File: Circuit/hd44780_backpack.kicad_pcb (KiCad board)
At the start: 2 copper layers, 98.4 x 60.3 mm, 32 parts, among them IC1 ATTINY84A-SS, K1 PWR_SHIFT, M1 MESHTHING, P1 I2C, P2 ISCP, P3 ATTINY_BREAKOUT, P4 USB_5PIN_SHELL, P5 MESH_BKOUT_1-10, P6 MESH_BKOUT_11-20, P7 MESH_ENABLE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

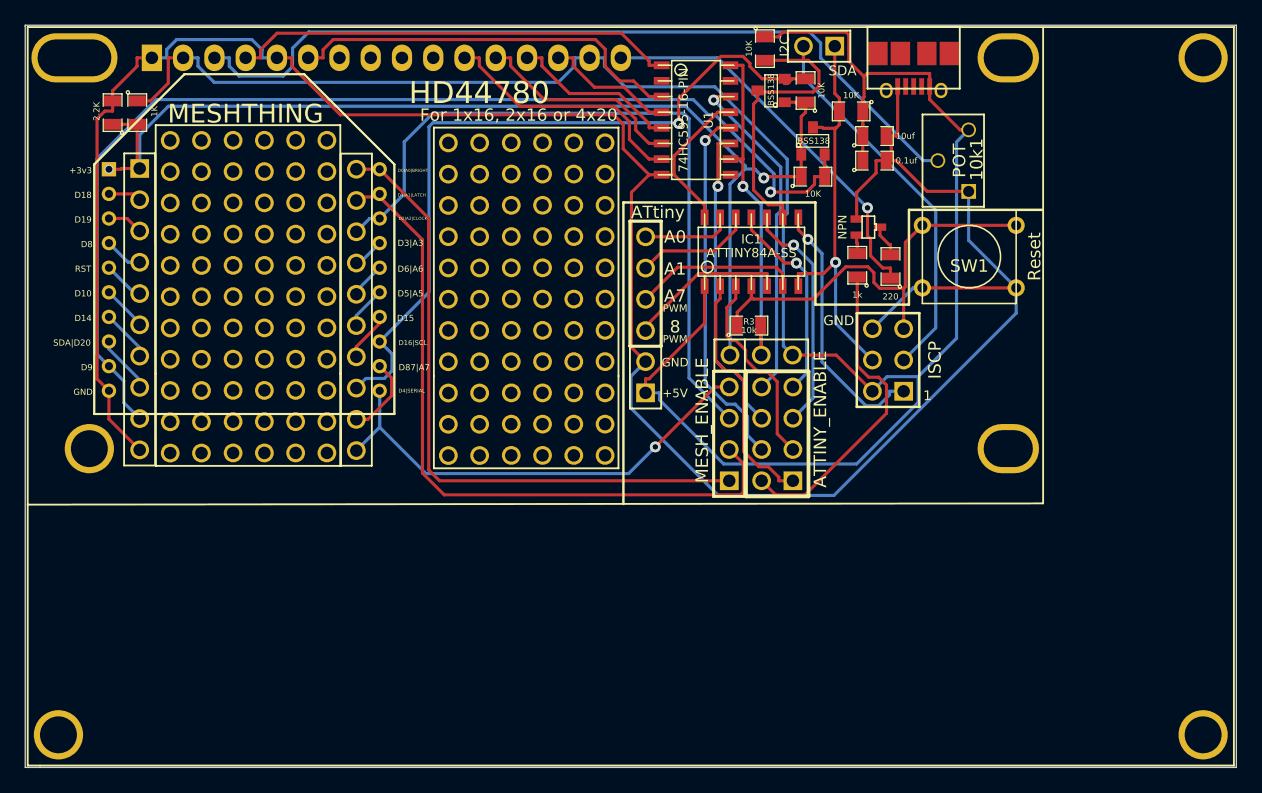
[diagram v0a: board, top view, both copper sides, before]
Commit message: Changed to using a BSS138DW
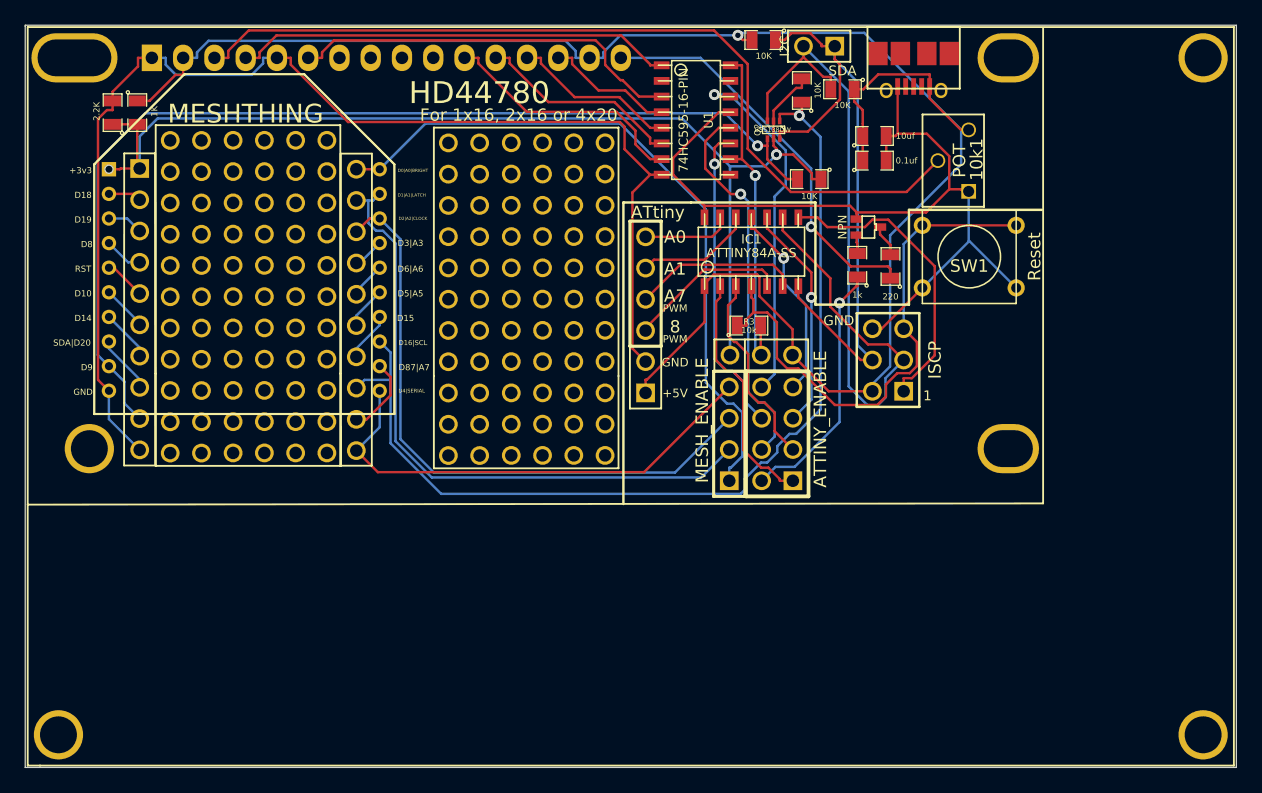
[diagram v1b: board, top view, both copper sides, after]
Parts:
- removed Q3: BSS138, SOT23
- Q2: value BSS138 -> BSS138DW; footprint SOT23 -> SOT363
- moved Q2 3.32 mm to (73.1, 20.8), turned to 180 degrees
- moved R4 1.93 mm to (78.7, 17.5)
- moved R6 0.71 mm to (72.3, 13.5), turned to 180 degrees
- moved R5 0.36 mm to (76.0, 24.8), turned to 180 degrees
- moved R7 0.30 mm to (75.4, 17.6)
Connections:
- IC1 pad 7: N-0000032 (its old number) -> N-0000055
- IC1 pad 9: N-0000019 (its old number) -> N-0000057
- M1 pad 13: N-0000022 (its old number) -> N-0000056
- M1 pad 9: N-0000033 (its old number) -> N-0000058
- P1 pad 1: N-0000032 (its old number) -> N-0000055
- P1 pad 2: N-0000019 (its old number) -> N-0000057
- P2 pad 3: N-0000019 (its old number) -> N-0000057
- P2 pad 4: N-0000032 (its old number) -> N-0000055
- P5 pad 2: N-0000033 (its old number) -> N-0000058
- P6 pad 8: N-0000022 (its old number) -> N-0000056
- Q2 pad 1: +3.3V -> N-0000056
- Q2 pad 2: N-0000033 (its old number) -> +3.3V
- Q2 pad 3: N-0000032 (its old number) -> N-0000057
- R4 pad 2: N-0000032 (its old number) -> N-0000057
- R5 pad 2: N-0000033 (its old number) -> N-0000058
- R6 pad 1: +5V -> N-0000055
- R6 pad 2: N-0000019 (its old number) -> +5V
- R7 pad 1: +3.3V -> N-0000056
- R7 pad 2: N-0000022 (its old number) -> +3.3V
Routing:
- net N-0000033 (its old number): track 90.7 -> 0.00 mm, vias 1 -> 0
- net N-0000058: track 0.00 -> 84.3 mm, vias 0 -> 1
- net N-0000056: track 0.00 -> 79.9 mm, vias 0 -> 1
- net N-0000057: track 0.00 -> 64.5 mm
- net N-0000022 (its old number): track 61.0 -> 0.00 mm, vias 1 -> 0
- net N-0000019 (its old number): track 55.6 -> 0.00 mm
- net N-0000055: track 0.00 -> 52.5 mm
- net N-0000032 (its old number): track 33.3 -> 0.00 mm, vias 1 -> 0
- net GND: track 204.5 -> 171.5 mm
- net +5V: track 181.2 -> 151.3 mm, vias 0 -> 1
- net N-0000023: track 35.1 -> 44.4 mm
- net N-0000033: track 59.4 -> 50.6 mm
- net N-000004: track 25.9 -> 20.7 mm, vias 0 -> 1
- net N-0000030: track 57.0 -> 52.2 mm
- net N-0000032: track 52.8 -> 56.9 mm
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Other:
- net class Default: clearance 0.254 -> 0.2; trace_width 0.254 -> 0.2
- rule trace_clearance: 0.254 -> 0.2
- rule trace_min: 0.254 -> 0.2

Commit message: problem with back masks
the meshthingy had no back mask area.  made it very difficult to solder.
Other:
- board text added: "Controller for HD4470 Screen Designed by John Spencer, 2014 https://github.com/mage0r/HD44780_Backpack Version 1.5 - Meshthingy Version"
- board text removed: "Controller for HD4470 Screen Designed by John Spencer, 2014 https://github.com/mage0r/HD44780_Backpack Version 1.4 - Meshthingy Version"
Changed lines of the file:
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@@
 (kicad_pcb (version 3) (host pcbnew "(2013-07-07 BZR 4022)-stable")
   (general
-    (links 101)
+    (links 0)
     (no_connects 0)
-    (area 12.249999 12.249999 110.750001 72.650001)
+    (area 12.05 10.575 110.775001 72.725001)
     (thickness 1.6)
     (drawings 18)
@@
     (15 F.Cu signal)
     (0 B.Cu signal)
-    (16 B.Adhes user)
-    (17 F.Adhes user)
+    (16 B.Adhes user hide)
+    (17 F.Adhes user hide)
     (18 B.Paste user)
     (19 F.Paste user)
@@
     (22 B.Mask user)
     (23 F.Mask user)
-    (24 Dwgs.User user)
-    (25 Cmts.User user)
-    (26 Eco1.User user)
-    (27 Eco2.User user)
-    (28 Edge.Cuts user)
+    (24 Dwgs.User user hide)
+    (25 Cmts.User user hide)
+    (26 Eco1.User user hide)
+    (27 Eco2.User user hide)
+    (28 Edge.Cuts user hide)
   )
   (setup
@@
     (mod_text_size 1 1)
     (mod_text_width 0.15)
-    (pad_size 1.524 1.524)
-    (pad_drill 1.016)
+    (pad_size 1.1684 1.1684)
+    (pad_drill 0.6604)
     (pad_to_mask_clearance 0)
     (aux_axis_origin 0 0)
@@
       (effects (font (size 1.778 1.778) (thickness 0.0889)))
     )
-    (fp_text value MESHTHING (at 0.1 -13.5) (layer F.SilkS)
+    (fp_text value MESHTHING (at 0 -14.4) (layer F.SilkS)
       (effects (font (size 1.524 1.524) (thickness 0.15)))
     )
@@
     )
     (pad 2 thru_hole circle (at -10.9982 -6.9977) (size 1.1684 1.1684) (drill 0.6604)
-      (layers *.Cu F.Paste F.SilkS F.Mask)
+      (layers *.Cu *.Mask F.Paste F.SilkS)
       (net 33 N-0000037)
     )
     (pad 3 thru_hole circle (at -10.9982 -4.99872) (size 1.1684 1.1684) (drill 0.6604)
-      (layers *.Cu F.Paste F.SilkS F.Mask)
+      (layers *.Cu *.Mask F.Paste F.SilkS)
       (net 34 N-0000038)
     )
     (pad 4 thru_hole circle (at -10.9982 -2.99974) (size 1.1684 1.1684) (drill 0.6604)
-      (layers *.Cu F.Paste F.SilkS F.Mask)
+      (layers *.Cu *.Mask F.Paste F.SilkS)
       (net 35 N-0000039)
     )
     (pad 5 thru_hole circle (at -10.9982 -0.99822) (size 1.1684 1.1684) (drill 0.6604)
-      (layers *.Cu F.Paste F.SilkS F.Mask)
+      (layers *.Cu *.Mask F.Paste F.SilkS)
       (net 31 N-0000035)
     )
     (pad 6 thru_hole circle (at -10.9982 0.99822) (size 1.1684 1.1684) (drill 0.6604)
-      (layers *.Cu F.Paste F.SilkS F.Mask)
+      (layers *.Cu *.Mask F.Paste F.SilkS)
       (net 37 N-0000040)
     )
     (pad 7 thru_hole circle (at -10.9982 2.99974) (size 1.1684 1.1684) (drill 0.6604)
-      (layers *.Cu F.Paste F.SilkS F.Mask)
+      (layers *.Cu *.Mask F.Paste F.SilkS)
       (net 38 N-0000041)
     )
     (pad 8 thru_hole circle (at -10.9982 4.99872) (size 1.1684 1.1684) (drill 0.6604)
-      (layers *.Cu F.Paste F.SilkS F.Mask)
+      (layers *.Cu *.Mask F.Paste F.SilkS)
       (net 39 N-0000042)
     )
     (pad 9 thru_hole circle (at -10.9982 6.9977) (size 1.1684 1.1684) (drill 0.6604)
-      (layers *.Cu F.Paste F.SilkS F.Mask)
+      (layers *.Cu *.Mask F.Paste F.SilkS)
       (net 44 N-0000058)
     )
     (pad 10 thru_hole circle (at -10.9982 8.99922) (size 1.1684 1.1684) (drill 0.6604)
-      (layers *.Cu F.Paste F.SilkS F.Mask)
+      (layers *.Cu *.Mask F.Paste F.SilkS)
       (net 3 GND)
     )
     (pad 11 thru_hole circle (at 10.9982 8.99922) (size 1.1684 1.1684) (drill 0.6604)
-      (layers *.Cu F.Paste F.SilkS F.Mask)
+      (layers *.Cu *.Mask F.Paste F.SilkS)
       (net 9 N-0000014)
     )
     (pad 12 thru_hole circle (at 10.9982 6.9977) (size 1.1684 1.1684) (drill 0.6604)
-      (layers *.Cu F.Paste F.SilkS F.Mask)
+      (layers *.Cu *.Mask F.Paste F.SilkS)
       (net 10 N-0000015)
     )
     (pad 13 thru_hole circle (at 10.9982 4.99872) (size 1.1684 1.1684) (drill 0.6604)
-      (layers *.Cu F.Paste F.SilkS F.Mask)
+      (layers *.Cu *.Mask F.Paste F.SilkS)
       (net 42 N-0000056)
     )
     (pad 14 thru_hole circle (at 10.9982 2.99974) (size 1.1684 1.1684) (drill 0.6604)
-      (layers *.Cu F.Paste F.SilkS F.Mask)
+      (layers *.Cu *.Mask F.Paste F.SilkS)
       (net 8 N-0000013)
     )
     (pad 15 thru_hole circle (at 10.9982 0.99822) (size 1.1684 1.1684) (drill 0.6604)
-      (layers *.Cu F.Paste F.SilkS F.Mask)
+      (layers *.Cu *.Mask F.Paste F.SilkS)
       (net 7 N-0000012)
     )
     (pad 16 thru_hole circle (at 10.9982 -0.99822) (size 1.1684 1.1684) (drill 0.6604)
-      (layers *.Cu F.Paste F.SilkS F.Mask)
+      (layers *.Cu *.Mask F.Paste F.SilkS)
       (net 30 N-0000034)
     )
     (pad 17 thru_hole circle (at 10.9982 -2.99974) (size 1.1684 1.1684) (drill 0.6604)
-      (layers *.Cu F.Paste F.SilkS F.Mask)
+      (layers *.Cu *.Mask F.Paste F.SilkS)
       (net 32 N-0000036)
     )
     (pad 18 thru_hole circle (at 10.9982 -4.99872) (size 1.1684 1.1684) (drill 0.6604)
-      (layers *.Cu F.Paste F.SilkS F.Mask)
+      (layers *.Cu *.Mask F.Paste F.SilkS)
       (net 29 N-0000033)
     )
     (pad 19 thru_hole circle (at 10.9982 -6.9977) (size 1.1684 1.1684) (drill 0.6604)
-      (layers *.Cu F.Paste F.SilkS F.Mask)
+      (layers *.Cu *.Mask F.Paste F.SilkS)
       (net 27 N-0000030)
     )
     (pad 20 thru_hole circle (at 10.9982 -8.99922) (size 1.1684 1.1684) (drill 0.6604)
-      (layers *.Cu F.Paste F.SilkS F.Mask)
+      (layers *.Cu *.Mask F.Paste F.SilkS)
       (net 28 N-0000032)
     )
@@
   (gr_line (start 12.3 72.6) (end 110.7 72.6) (angle 90) (layer Edge.Cuts) (width 0.1))
   (gr_line (start 12.3 12.4) (end 12.3 72.6) (angle 90) (layer Edge.Cuts) (width 0.1))
-  (gr_text "Controller for HD4470 Screen\nDesigned by John Spencer, 2014\nhttps://github.com/mage0r/HD44780_Backpack\nVersion 1.4 - Meshthingy Version" (at 75.5 22) (layer B.SilkS)
+  (gr_text "Controller for HD4470 Screen\nDesigned by John Spencer, 2014\nhttps://github.com/mage0r/HD44780_Backpack\nVersion 1.5 - Meshthingy Version" (at 75.5 22) (layer B.SilkS)
     (effects (font (size 0.8 0.8) (thickness 0.2)) (justify mirror))
   )
